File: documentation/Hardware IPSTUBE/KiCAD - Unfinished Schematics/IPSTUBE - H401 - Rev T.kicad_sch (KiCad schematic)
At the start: 67 parts, among them J1 Conn_Coaxial_Small, P1 USB_C_Plug, Q2 AO3401A, SW1 Reset Switch, U1 CH340N, U2 ESP32-PICO-D4, U4 DS1302Z+, U5 AT25SF081-SSHD-X, U6 MI6118, X1 Crystal, X3 Crystal

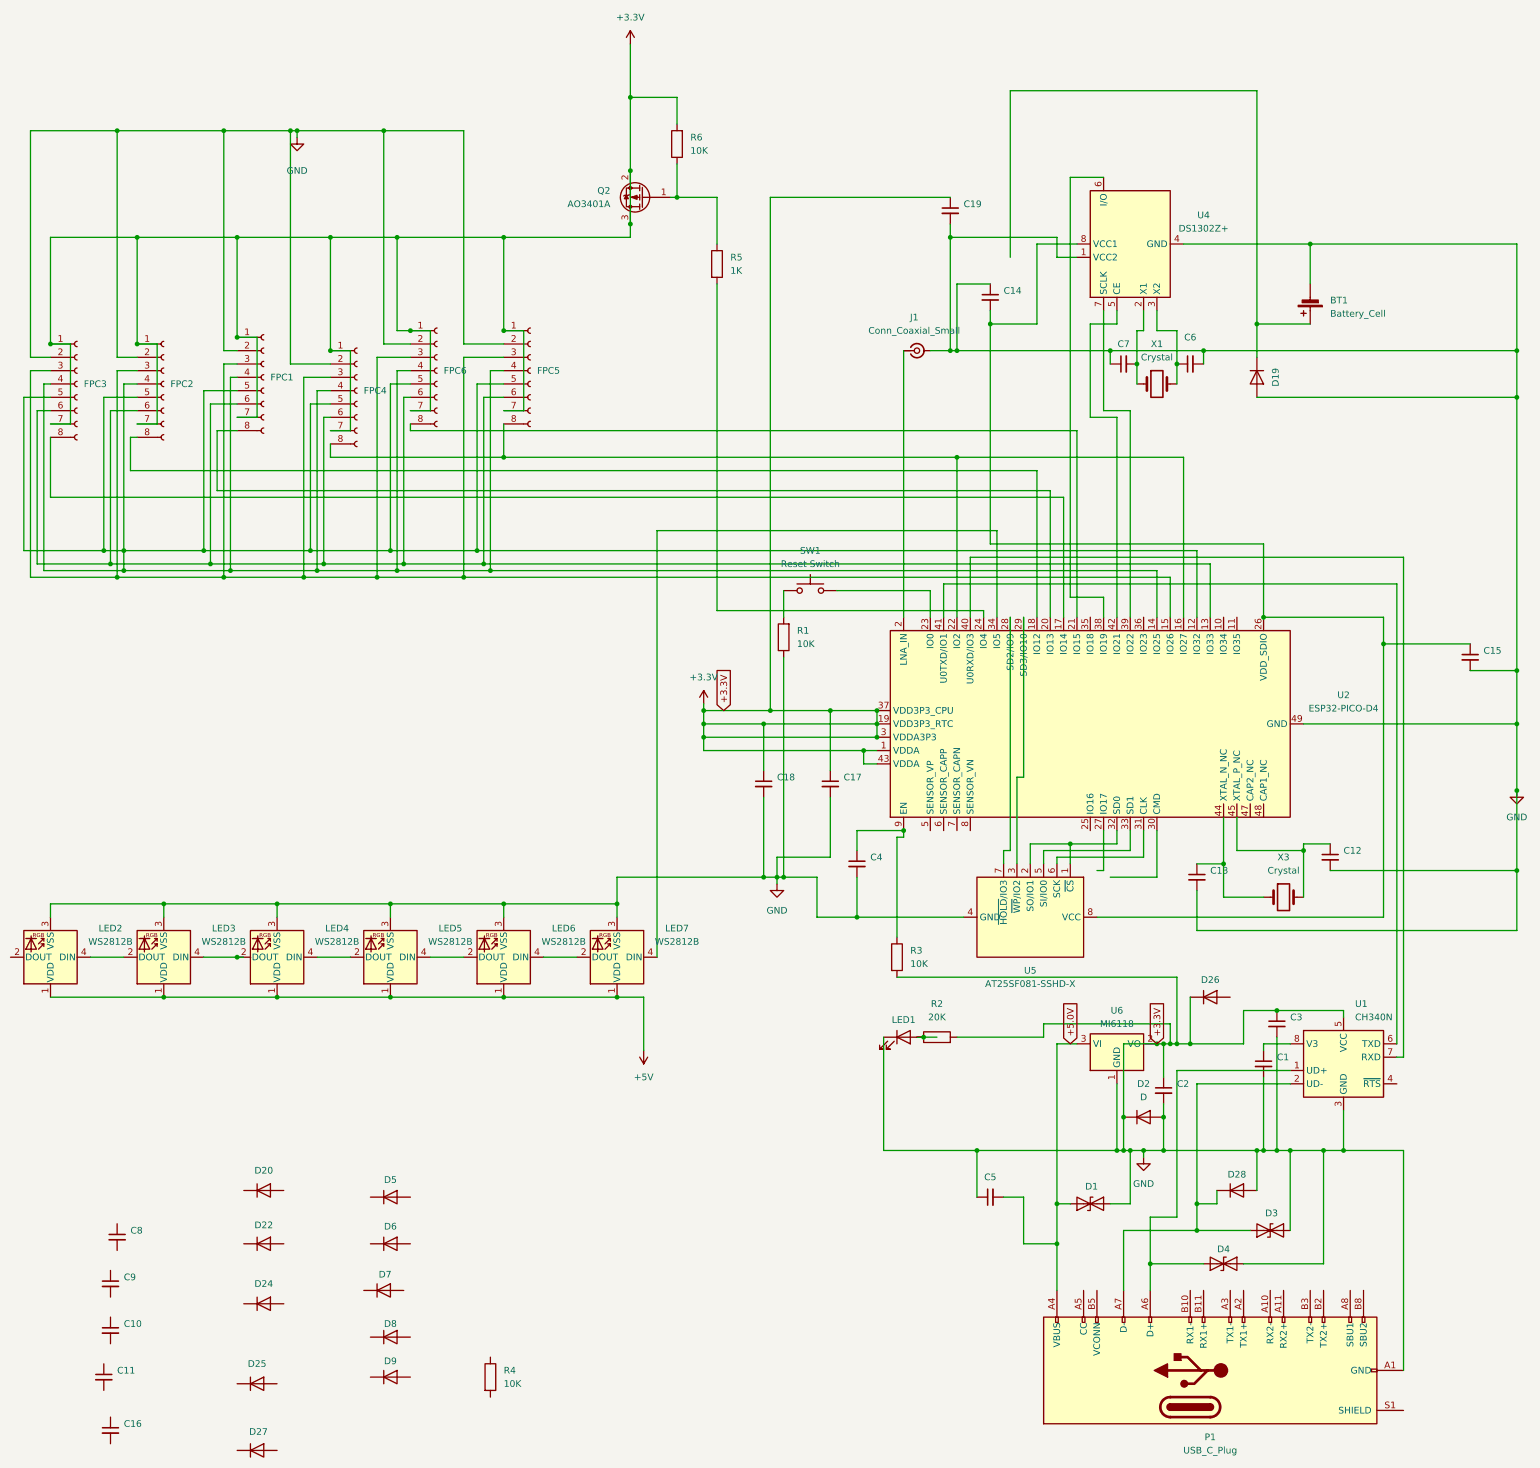
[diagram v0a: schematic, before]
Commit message: Refactor code for IPSTUBEs
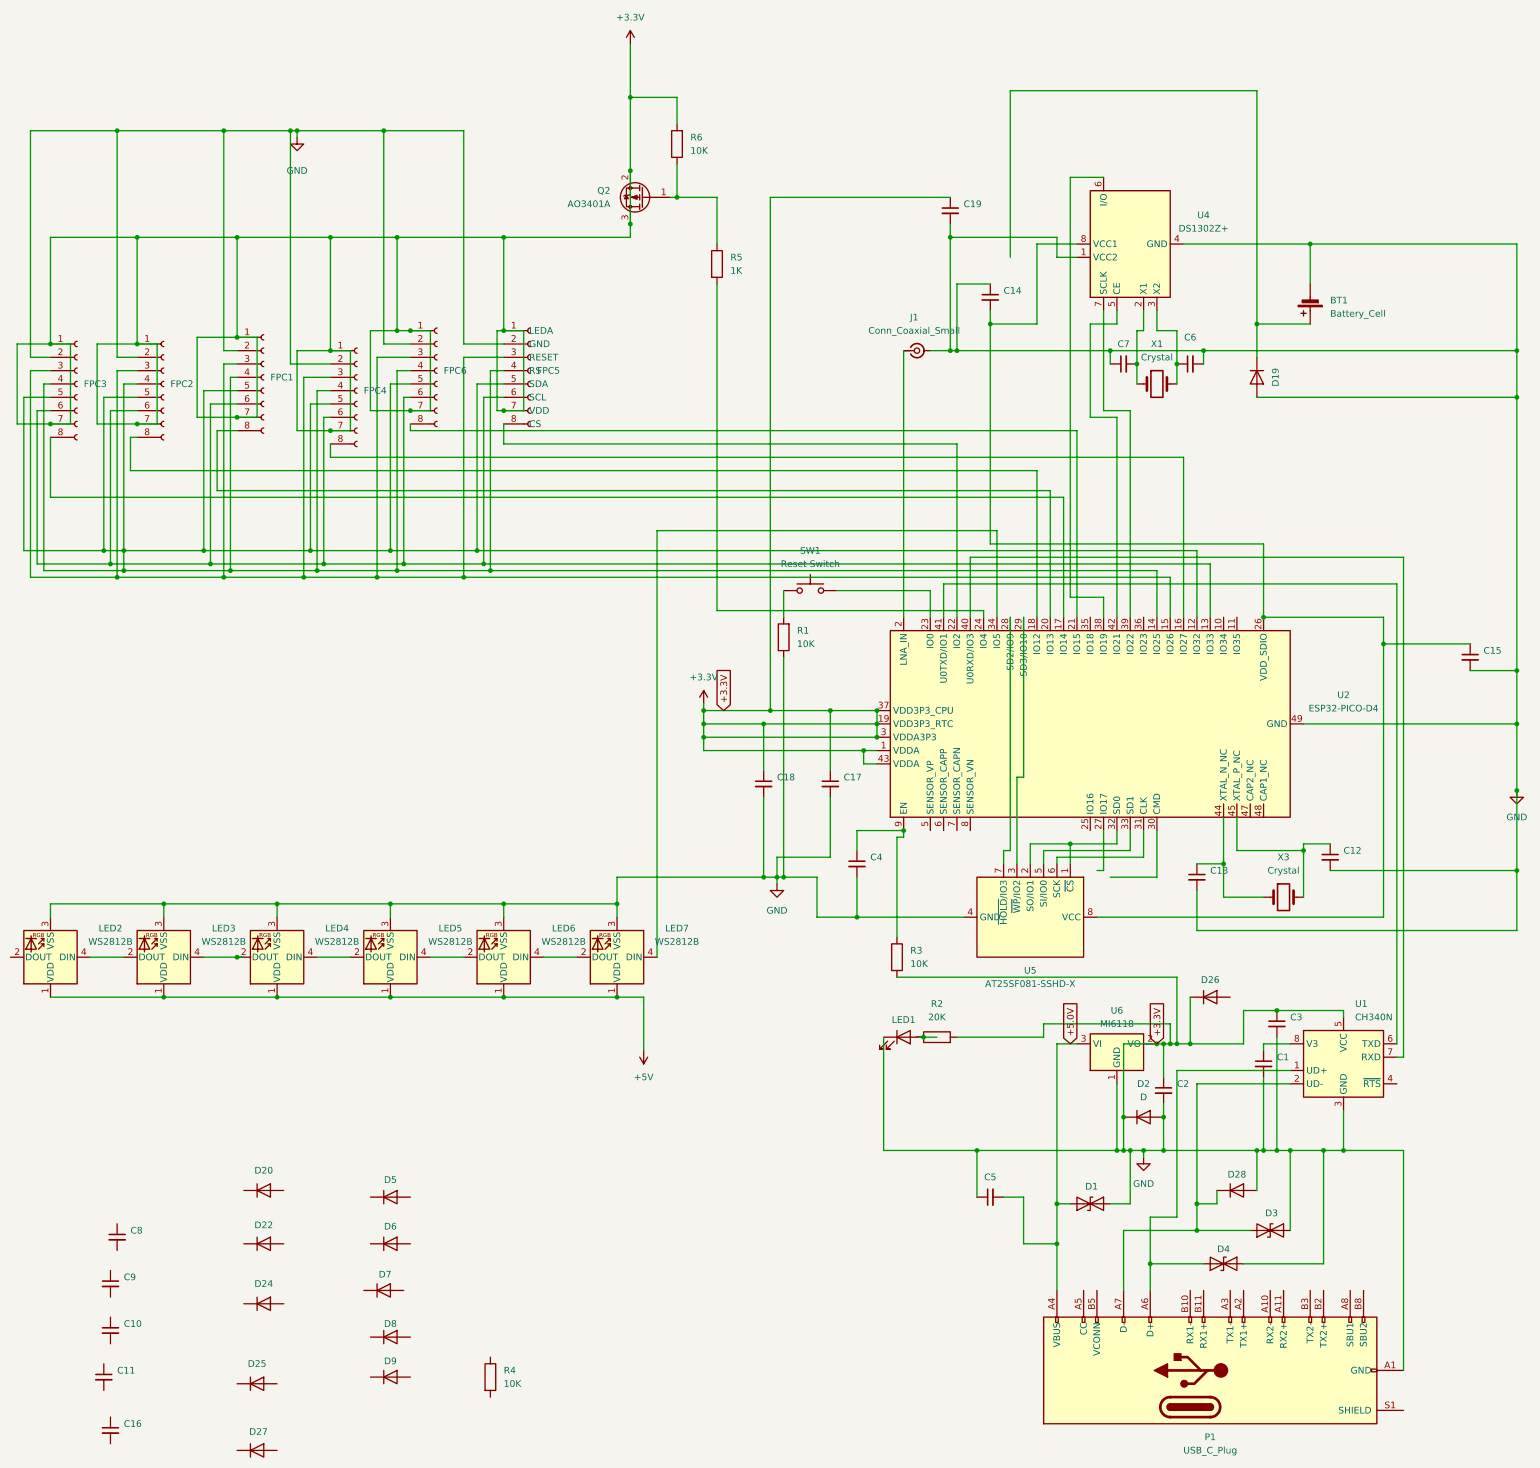
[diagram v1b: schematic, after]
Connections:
- net at FPC5.8 (CS), U2.22 (IO2): no longer FPC4.8 (Pin_8), U2.16 (IO27)
- new net: FPC4.8 (Pin_8), U2.16 (IO27)
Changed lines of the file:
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@@
 (kicad_sch
-	(version 20231120)
+	(version 20250114)
 	(generator "eeschema")
-	(generator_version "8.0")
+	(generator_version "9.0")
 	(paper "A4")
 	(junction
@@
 	)
 	(junction
+		(at 74.93 -5.08)
+		(diameter 0)
+		(color 0 0 0 0)
+	)
+	(junction
 		(at 57.15 -41.91)
 		(diameter 0)
@@
 	)
 	(junction
+		(at 87.63 -24.13)
+		(diameter 0)
+		(color 0 0 0 0)
+	)
+	(junction
 		(at 43.18 85.09)
 		(diameter 0)
@@
 	)
 	(junction
+		(at 57.15 -7.62)
+		(diameter 0)
+		(color 0 0 0 0)
+	)
+	(junction
 		(at 31.75 17.78)
 		(diameter 0)
@@
 	)
 	(junction
+		(at 21.59 -6.35)
+		(diameter 0)
+		(color 0 0 0 0)
+	)
+	(junction
 		(at 228.6 -17.78)
 		(diameter 0)
@@
 	)
 	(junction
+		(at 90.17 -8.89)
+		(diameter 0)
+		(color 0 0 0 0)
+	)
+	(junction
 		(at 107.95 85.09)
 		(diameter 0)
@@
 	)
 	(junction
-		(at 107.95 0)
-		(diameter 0)
-		(color 0 0 0 0)
-	)
-	(junction
 		(at 232.41 111.76)
 		(diameter 0)
@@
 	)
 	(junction
-		(at 194.31 0)
-		(diameter 0)
-		(color 0 0 0 0)
-	)
-	(junction
 		(at 105.41 21.59)
 		(diameter 0)
@@
 	)
 	(junction
+		(at 107.95 -8.89)
+		(diameter 0)
+		(color 0 0 0 0)
+	)
+	(junction
 		(at 300.99 -20.32)
 		(diameter 0)
@@
 	)
 	(junction
+		(at 38.1 -6.35)
+		(diameter 0)
+		(color 0 0 0 0)
+	)
+	(junction
 		(at 176.53 55.88)
 		(diameter 0)
@@
 	(wire
 		(pts
+			(xy 194.31 30.48) (xy 194.31 -2.54)
+		)
+		(stroke
+			(width 0)
+			(type default)
+		)
+	)
+	(wire
+		(pts
 			(xy 140.97 -55.88) (xy 140.97 -49.53)
 		)
@@
 	(wire
 		(pts
-			(xy 237.49 0) (xy 194.31 0)
+			(xy 74.93 0) (xy 237.49 0)
 		)
 		(stroke
@@
 	(wire
 		(pts
+			(xy 194.31 -2.54) (xy 107.95 -2.54)
+		)
+		(stroke
+			(width 0)
+			(type default)
+		)
+	)
+	(wire
+		(pts
 			(xy 236.22 -24.13) (xy 236.22 -17.78)
 		)
@@
 	(wire
 		(pts
-			(xy 107.95 0) (xy 74.93 0)
-		)
-		(stroke
-			(width 0)
-			(type default)
-		)
-	)
-	(wire
-		(pts
 			(xy 19.05 20.32) (xy 33.02 20.32)
 		)
@@
 	(wire
 		(pts
+			(xy 106.68 -24.13) (xy 107.95 -24.13)
+		)
+		(stroke
+			(width 0)
+			(type default)
+		)
+	)
+	(wire
+		(pts
 			(xy 252.73 132.08) (xy 255.27 132.08)
 		)
@@
 	(wire
 		(pts
+			(xy 68.58 -20.32) (xy 74.93 -20.32)
+		)
+		(stroke
+			(width 0)
+			(type default)
+		)
+	)
+	(wire
+		(pts
 			(xy 237.49 30.48) (xy 237.49 0)
 		)
@@
 	(wire
 		(pts
+			(xy 15.24 -21.59) (xy 21.59 -21.59)
+		)
+		(stroke
+			(width 0)
+			(type default)
+		)
+	)
+	(wire
+		(pts
 			(xy 215.9 -53.34) (xy 222.25 -53.34)
 		)
@@
 	(wire
 		(pts
+			(xy 82.55 -24.13) (xy 87.63 -24.13)
+		)
+		(stroke
+			(width 0)
+			(type default)
+		)
+	)
+	(wire
+		(pts
 			(xy 208.28 73.66) (xy 208.28 77.47)
 		)
@@
 	(wire
 		(pts
-			(xy 191.77 24.13) (xy 191.77 30.48)
+			(xy 82.55 -8.89) (xy 82.55 -24.13)
 		)
 		(stroke
@@
 	(wire
 		(pts
-			(xy 107.95 -6.35) (xy 107.95 0)
+			(xy 191.77 24.13) (xy 191.77 30.48)
 		)
 		(stroke
@@
 	(wire
 		(pts
+			(xy 30.48 -6.35) (xy 30.48 -21.59)
+		)
+		(stroke
+			(width 0)
+			(type default)
+		)
+	)
+	(wire
+		(pts
 			(xy 226.06 158.75) (xy 226.06 147.32)
 		)
@@
 	(wire
 		(pts
+			(xy 107.95 -6.35) (xy 107.95 -2.54)
+		)
+		(stroke
+			(width 0)
+			(type default)
+		)
+	)
+	(wire
+		(pts
 			(xy 50.8 95.25) (xy 57.15 95.25)
 		)
@@
 	(wire
 		(pts
+			(xy 106.68 -8.89) (xy 107.95 -8.89)
+		)
+		(stroke
+			(width 0)
+			(type default)
+		)
+	)
+	(wire
+		(pts
 			(xy 146.05 50.8) (xy 157.48 50.8)
 		)
@@
 	(wire
 		(pts
-			(xy 107.95 -8.89) (xy 111.76 -8.89)
+			(xy 236.22 144.78) (xy 236.22 116.84)
 		)
 		(stroke
@@
 	(wire
 		(pts
-			(xy 236.22 144.78) (xy 236.22 116.84)
+			(xy 15.24 -6.35) (xy 15.24 -21.59)
 		)
 		(stroke
@@
 	(wire
 		(pts
+			(xy 107.95 -8.89) (xy 111.76 -8.89)
+		)
+		(stroke
+			(width 0)
+			(type default)
+		)
+	)
+	(wire
+		(pts
 			(xy 38.1 -21.59) (xy 38.1 -41.91)
 		)
@@
 	(wire
 		(pts
-			(xy 194.31 0) (xy 107.95 0)
+			(xy 212.09 30.48) (xy 212.09 6.35)
 		)
 		(stroke
@@
 	(wire
 		(pts
-			(xy 212.09 30.48) (xy 212.09 6.35)
+			(xy 106.68 -8.89) (xy 106.68 -24.13)
 		)
 		(stroke
@@
 	(wire
 		(pts
+			(xy 74.93 -5.08) (xy 68.58 -5.08)
+		)
+		(stroke
+			(width 0)
+			(type default)
+		)
+	)
+	(wire
+		(pts
 			(xy 217.17 -5.08) (xy 217.17 30.48)
 		)
@@
 	(wire
 		(pts
+			(xy 90.17 -8.89) (xy 82.55 -8.89)
+		)
+		(stroke
+			(width 0)
+			(type default)
+		)
+	)
+	(wire
+		(pts
 			(xy 264.16 153.67) (xy 264.16 132.08)
 		)
@@
 	(wire
 		(pts
+			(xy 57.15 -7.62) (xy 49.53 -7.62)
+		)
+		(stroke
+			(width 0)
+			(type default)
+		)
+	)
+	(wire
+		(pts
 			(xy 265.43 73.66) (xy 260.35 73.66)
 		)
@@
 	(wire
 		(pts
+			(xy 21.59 -6.35) (xy 15.24 -6.35)
+		)
+		(stroke
+			(width 0)
+			(type default)
+		)
+	)
+	(wire
+		(pts
 			(xy 204.47 30.48) (xy 204.47 74.93)
 		)
@@
 	(wire
 		(pts
+			(xy 68.58 -5.08) (xy 68.58 -20.32)
+		)
+		(stroke
+			(width 0)
+			(type default)
+		)
+	)
+	(wire
+		(pts
 			(xy 132.08 -54.61) (xy 132.08 -68.58)
 		)
@@
 	(wire
 		(pts
+			(xy 38.1 -6.35) (xy 30.48 -6.35)
+		)
+		(stroke
+			(width 0)
+			(type default)
+		)
+	)
+	(wire
+		(pts
 			(xy 209.55 -25.4) (xy 209.55 -40.64)
 		)
@@
 	(wire
 		(pts
+			(xy 49.53 -7.62) (xy 49.53 -22.86)
+		)
+		(stroke
+			(width 0)
+			(type default)
+		)
+	)
+	(wire
+		(pts
 			(xy 21.59 85.09) (xy 21.59 87.63)
 		)
@@
 	(wire
 		(pts
+			(xy 30.48 -21.59) (xy 38.1 -21.59)
+		)
+		(stroke
+			(width 0)
+			(type default)
+		)
+	)
+	(wire
+		(pts
 			(xy 171.45 25.4) (xy 189.23 25.4)
 		)
@@
 	(wire
 		(pts
-			(xy 194.31 30.48) (xy 194.31 0)
+			(xy 49.53 -22.86) (xy 57.15 -22.86)
 		)
 		(stroke
@@
 	)
 	(symbol
+		(lib_name "Conn_01x08_Socket_1")
 		(lib_id "Connector:Conn_01x08_Socket")
 		(at 113.03 -16.51 0)
@@
 		)
 	)
+	(embedded_fonts no)
 )
